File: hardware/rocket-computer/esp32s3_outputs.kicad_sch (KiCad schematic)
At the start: 43 parts, among them J5 Conn_01x04, SW3 R-667995, U11 GD5F2GQ5UEYIGR, U13 GD25Q128ESIG, U14 479480001, U15 ESP32-S3RH2, U29 TPS22810DRVR, Y1 ABS07-32.768KHZ-T, Y2 ECS-400-10-37B2-CKY-TR

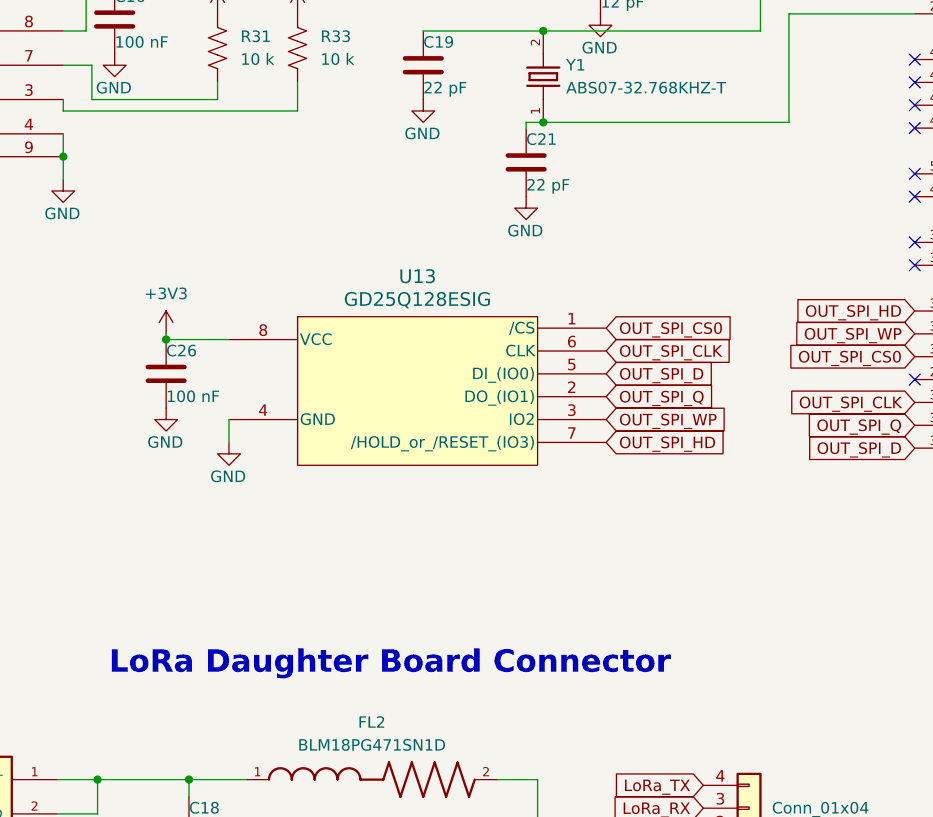
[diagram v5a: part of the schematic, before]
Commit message: hardware(V10): the part swaps the mini got and this board never did — both boot NORs, the pyro FETs, the magnetometer and the barometer (#1452)
v10-power-parity-2026-09-11.md closed the *circuit* differences between the
two boards, measuring forward from the TPS61094 rework (2026-08-29). It never
looked further back, and the *part* swaps in a4667604 (2026-08-16,
"hardware(minis): cost-reduction part swaps") only ever touched the two mini
boards. Two of that commit's six items had since arrived here by other routes
(DTC123JETL on 09-05, the PA0805 shunt); the rest had not.

Carried over:

- U13/U16 boot NOR: GD25Q128ESIG SOIC-8 208 mil -> W25Q128JVYIQ 24-ball WLCSP,
  the part the mini moved to on 2026-09-04. Both placements keep every net;
  only the pad names change (1-8 -> ball designators). Both blocks redrawn so
  the pins land on their labels, and U16's /CS pull-up R46 now runs over the
  top of the part into the VCC node.
- U6/U7/U8/U10 pyro high-side P-FETs: TPN4R712MD -> Winsok WSD20L50DN33. The
  incumbent is unbuyable at build quantity until the Q4-2026 Mouser restock;
  land compatibility was closed on the mini by numeric overlay of the vendor
  drawing. Same footprint, same 8-pin geometry, pins typed passive instead of
  unspecified.
- U9 pyro-ARM N-FET: CSD16323Q3 -> AOS AON7534. Same pinout, same land, and
  the mini keeps the CSD16323Q3 symbol for it, so this is fields only.
- U3 magnetometer: IIS2MDCTR LGA-12 2x2 -> QST QMC5883P LGA-16 3x3, with C6
  220 nF -> 10 uF for the C1 reservoir. Not pad-for-pad: IIS2MDCTR_SCL/SDA
  become MAG_SCL/MAG_SDA (the mini's names — they name the slot, not the part
  in it), the QMC land exposes no DRDY/INT pad so IIS2MDCTR_INT is gone and P4
  GPIO46 is free with a no-connect on it, and the ST part's separate VDD_IO and
  its CS strap to V_MCU_SWTCH go with it.
- U4 barometer: BMP585 LGA-9 -> BMP581 LGA-10 2x2. A drop-in on the drawing —
  the two symbols are built to the same pin grid, so U4 keeps its placement and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
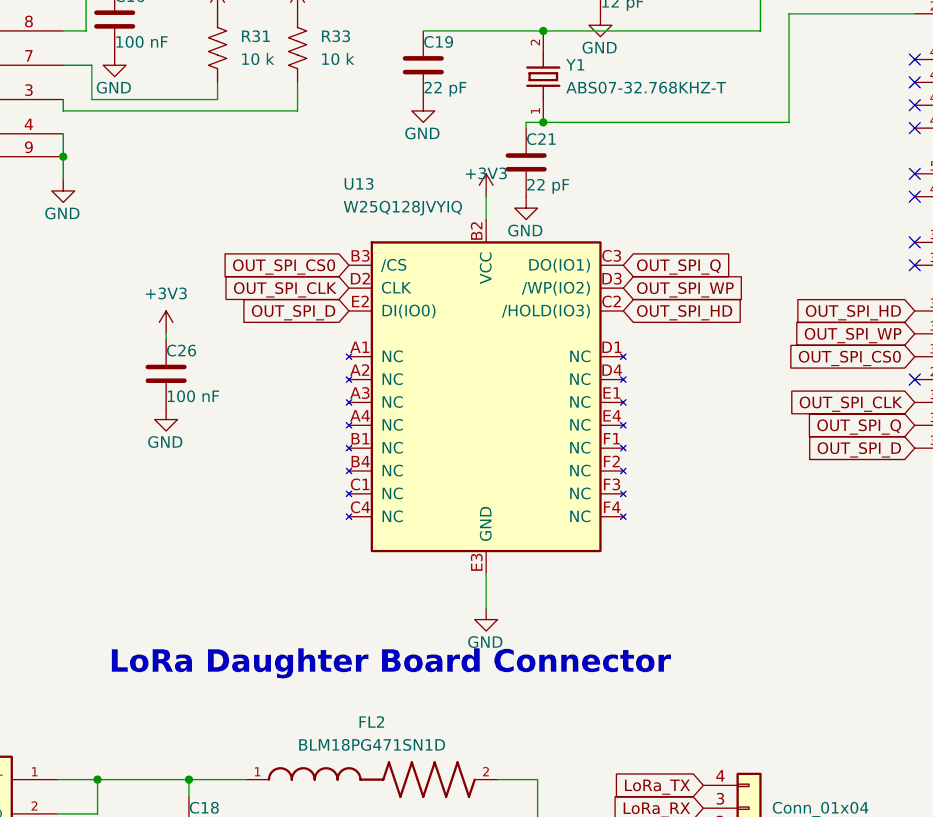
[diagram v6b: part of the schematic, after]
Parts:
- C18: MPN CL21A226MOQNNNE -> CL21A226KOQNNNE
- U13: value GD25Q128ESIG -> W25Q128JVYIQ; footprint Footprints:SOIC127P790X216-8N -> Footprints:24-WLCSP_Y_WIN; symbol Custom:W25Q128JVSIQ -> Custom:W25Q128JVYIQ; MPN GD25Q128ESIG -> W25Q128JVYIQ; Mfr GigaDevice -> Winbond
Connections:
- net +3V3: now also U13.B2 (VCC); no longer U13.8 (VCC)
- net GND: now also U13.E3 (GND); no longer U13.4 (GND)
- net OUT_SPI_CLK: now also U13.D2 (CLK); no longer U13.6 (CLK)
- net OUT_SPI_CS0: now also U13.B3 (/CS); no longer U13.1 (/CS)
- net OUT_SPI_D: now also U13.E2 (DI(IO0)); no longer U13.5 (DI_(IO0))
- net OUT_SPI_HD: now also U13.C2 (/HOLD(IO3)); no longer U13.7 (/HOLD_or_/RESET_(IO3))
- net OUT_SPI_Q: now also U13.C3 (DO(IO1)); no longer U13.2 (DO_(IO1))
- net OUT_SPI_WP: now also U13.D3 (/WP(IO2)); no longer U13.3 (IO2)
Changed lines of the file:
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@@
 		(color 0 0 0 0)
 	)
-	(junction
-		(at 78.74 104.775)
-		(diameter 0)
-		(color 0 0 0 0)
-	)
 	(wire
 		(pts
@@
 	(wire
 		(pts
-			(xy 85.725 113.665) (xy 85.725 116.205)
-		)
-		(stroke
-			(width 0)
-			(type default)
-		)
-	)
-	(wire
-		(pts
 			(xy 81.28 153.67) (xy 87.63 153.67)
 		)
@@
 	(wire
 		(pts
-			(xy 78.74 104.775) (xy 85.725 104.775)
-		)
-		(stroke
-			(width 0)
-			(type default)
-		)
-	)
-	(wire
-		(pts
 			(xy 161.925 66.04) (xy 144.78 66.04)
 		)
@@
 	(global_label "OUT_SPI_CS0"
 		(shape input)
-		(at 127.635 103.505 0)
+		(at 99.06 96.52 180)
 		(fields_autoplaced yes)
 		(effects
@@
 				(size 1.27 1.27)
 			)
-			(justify left)
+			(justify right)
 		)
 		(property "Intersheetrefs" "${INTERSHEET_REFS}"
-			(at 142.9573 103.505 0)
+			(at 83.7377 96.52 0)
 			(hide yes)
 			(show_name no)
@@
 					(size 1.27 1.27)
 				)
-				(justify left)
+				(justify right)
 			)
 		)
@@
 	(global_label "OUT_SPI_CLK"
 		(shape input)
-		(at 127.635 106.045 0)
+		(at 99.06 99.06 180)
 		(fields_autoplaced yes)
 		(effects
@@
 				(size 1.27 1.27)
 			)
-			(justify left)
+			(justify right)
 		)
 		(property "Intersheetrefs" "${INTERSHEET_REFS}"
-			(at 142.8364 106.045 0)
+			(at 83.8586 99.06 0)
 			(hide yes)
 			(show_name no)
@@
 					(size 1.27 1.27)
 				)
-				(justify left)
+				(justify right)
 			)
 		)
@@
 	(global_label "OUT_SPI_WP"
 		(shape input)
-		(at 127.635 113.665 0)
+		(at 129.54 99.06 0)
 		(fields_autoplaced yes)
 		(effects
@@
 		)
 		(property "Intersheetrefs" "${INTERSHEET_REFS}"
-			(at 141.9897 113.665 0)
+			(at 143.8947 99.06 0)
 			(hide yes)
 			(show_name no)
@@
 	(global_label "OUT_SPI_Q"
 		(shape input)
-		(at 127.635 111.125 0)
+		(at 129.54 96.52 0)
 		(fields_autoplaced yes)
 		(effects
@@
 		)
 		(property "Intersheetrefs" "${INTERSHEET_REFS}"
-			(at 140.5988 111.125 0)
+			(at 142.5038 96.52 0)
 			(hide yes)
 			(show_name no)
@@
 	(global_label "OUT_SPI_D"
 		(shape input)
-		(at 127.635 108.585 0)
+		(at 99.06 101.6 180)
 		(fields_autoplaced yes)
 		(effects
@@
 				(size 1.27 1.27)
 			)
-			(justify left)
+			(justify right)
 		)
 		(property "Intersheetrefs" "${INTERSHEET_REFS}"
-			(at 140.5383 108.585 0)
+			(at 86.1567 101.6 0)
 			(hide yes)
 			(show_name no)
@@
 					(size 1.27 1.27)
 				)
-				(justify left)
+				(justify right)
 			)
 		)
@@
 	(global_label "OUT_SPI_HD"
 		(shape input)
-		(at 127.635 116.205 0)
+		(at 129.54 101.6 0)
 		(fields_autoplaced yes)
 		(effects
@@
 		)
 		(property "Intersheetrefs" "${INTERSHEET_REFS}"
-			(at 141.8688 116.205 0)
+			(at 143.7738 101.6 0)
 			(hide yes)
 			(show_name no)
@@
 		)
 	)
-	(symbol
-		(lib_id "Custom:W25Q128JVSIQ")
-		(at 62.865 109.855 0)
+		(symbol
+		(lib_id "Custom:W25Q128JVYIQ")
+		(at 114.3 104.14 0)
 		(unit 1)
 		(body_style 1)
@@
 		(in_pos_files yes)
 		(dnp no)
-		(fields_autoplaced yes)
 		(property "Reference" "U13"
-			(at 106.68 97.79 0)
+			(at 98.425 88.265 0)
 			(show_name no)
 			(do_not_autoplace no)
 			(effects
 				(font
-					(size 1.524 1.524)
+					(size 1.27 1.27)
 				)
+				(justify left bottom)
 			)
 		)
-		(property "Value" "GD25Q128ESIG"
-			(at 106.68 100.33 0)
+		(property "Value" "W25Q128JVYIQ"
+			(at 98.425 90.805 0)
 			(show_name no)
 			(do_not_autoplace no)
 			(effects
 				(font
-					(size 1.524 1.524)
+					(size 1.27 1.27)
 				)
+				(justify left bottom)
 			)
 		)
-		(property "Footprint" "Footprints:SOIC127P790X216-8N"
-			(at 62.865 109.855 0)
+		(property "Footprint" "Footprints:24-WLCSP_Y_WIN"
+			(at 127 102.87 0)
 			(hide yes)
 			(show_name no)
@@
 				(font
 					(size 1.27 1.27)
-					(italic yes)
 				)
+				(justify left bottom)
 			)
 		)
 		(property "Datasheet" ""
-			(at 62.865 109.855 0)
+			(at 114.3 104.14 0)
 			(hide yes)
 			(show_name no)
@@
 				(font
 					(size 1.27 1.27)
-					(italic yes)
 				)
+				(justify left bottom)
 			)
 		)
-		(property "Description" ""
-			(at 62.865 109.855 0)
+		(property "Description" "128 Mbit serial NOR flash, quad SPI, 2.7-3.6 V, 24-ball WLCSP"
+			(at 114.3 104.14 0)
 			(hide yes)
 			(show_name no)
@@
 					(size 1.27 1.27)
 				)
+				(justify left bottom)
 			)
 		)
-		(property "MPN" "GD25Q128ESIG"
-			(at 62.865 109.855 0)
+		(property "MPN" "W25Q128JVYIQ"
+			(at 114.3 104.14 0)
 			(hide yes)
 			(show_name no)
@@
 					(size 1.27 1.27)
 				)
+				(justify left bottom)
 			)
 		)
-		(property "Mfr" "GigaDevice"
-			(at 62.865 109.855 0)
+		(property "Mfr" "Winbond"
+			(at 114.3 104.14 0)
 			(hide yes)
 			(show_name no)
@@
 					(size 1.27 1.27)
 				)
+				(justify left bottom)
 			)
 		)
-		(pin "8"
+		(pin "A1"
 		)
-		(pin "4"
+		(pin "A2"
 		)
-		(pin "2"
+		(pin "A3"
 		)
-		(pin "3"
+		(pin "A4"
 		)
-		(pin "5"
+		(pin "B1"
 		)
-		(pin "6"
+		(pin "B2"
 		)
-		(pin "7"
+		(pin "B3"
 		)
-		(pin "1"
+		(pin "B4"
+		)
+		(pin "C1"
+		)
+		(pin "C2"
+		)
+		(pin "C3"
+		)
+		(pin "C4"
+		)
+		(pin "D1"
+		)
+		(pin "D2"
+		)
+		(pin "D3"
+		)
+		(pin "D4"
+		)
+		(pin "E1"
+		)
+		(pin "E2"
+		)
+		(pin "E3"
+		)
+		(pin "E4"
+		)
+		(pin "F1"
+		)
+		(pin "F2"
+		)
+		(pin "F3"
+		)
+		(pin "F4"
 		)
 		(instances
@@
 	(symbol
 		(lib_id "power:GND")
-		(at 85.725 116.205 0)
+		(at 114.3 134.62 0)
 		(unit 1)
 		(body_style 1)
@@
 		(dnp no)
 		(property "Reference" "#PWR054"
-			(at 85.725 122.555 0)
+			(at 114.3 140.97 0)
 			(hide yes)
 			(show_name no)
@@
 		)
 		(property "Value" "GND"
-			(at 87.63 120.015 0)
+			(at 116.205 138.43 0)
 			(show_name no)
 			(do_not_autoplace no)
@@
 		)
 		(property "Footprint" ""
-			(at 85.725 116.205 0)
+			(at 114.3 134.62 0)
 			(hide yes)
 			(show_name no)
@@
 		)
 		(property "Datasheet" ""
-			(at 85.725 116.205 0)
+			(at 114.3 134.62 0)
 			(hide yes)
 			(show_name no)
@@
 		)
 		(property "Description" "Power symbol creates a global label with name \"GND\" , ground"
-			(at 85.725 116.205 0)
+			(at 114.3 134.62 0)
 			(hide yes)
 			(show_name no)
@@
 			)
 		)
-		(property "MPN" "CL21A226MOQNNNE"
+		(property "MPN" "CL21A226KOQNNNE"
 			(at 81.28 159.385 0)
 			(hide yes)
@@
 		(at 161.925 86.36)
 	)
+	(wire
+		(pts
+			(xy 114.3 130.81) (xy 114.3 134.62)
+		)
+		(stroke
+			(width 0)
+			(type default)
+		)
+	)
+	(wire
+		(pts
+			(xy 114.3 91.44) (xy 114.3 88.9)
+		)
+		(stroke
+			(width 0)
+			(type default)
+		)
+	)
+	(symbol
+		(lib_id "power:+3V3")
+		(at 114.3 88.9 0)
+		(unit 1)
+		(body_style 1)
+		(exclude_from_sim no)
+		(in_bom yes)
+		(on_board yes)
+		(in_pos_files yes)
+		(dnp no)
+		(fields_autoplaced yes)
+		(property "Reference" "#PWR0712"
+			(at 114.3 85.344 0)
+			(hide yes)
+			(show_name no)
+			(do_not_autoplace no)
+			(effects
+				(font
+					(size 1.27 1.27)
+				)
+			)
+		)
+		(property "Value" "+3V3"
+			(at 114.3 86.36 0)
+			(show_name no)
+			(do_not_autoplace no)
+			(effects
+				(font
+					(size 1.27 1.27)
+				)
+			)
+		)
+		(property "Footprint" ""
+			(at 114.3 88.9 0)
+			(hide yes)
+			(show_name no)
+			(do_not_autoplace no)
+			(effects
+				(font
+					(size 1.27 1.27)
+				)
+			)
+		)
+		(property "Datasheet" ""
+			(at 114.3 88.9 0)
+			(hide yes)
+			(show_name no)
+			(do_not_autoplace no)
+			(effects
+				(font
+					(size 1.27 1.27)
+				)
+			)
+		)
+		(property "Description" ""
+			(at 114.3 88.9 0)
+			(hide yes)
+			(show_name no)
+			(do_not_autoplace no)
+			(effects
+				(font
+					(size 1.27 1.27)
+				)
+			)
+		)
+		(pin "1"
+		)
+		(instances
+			(project "rocket-computer"
+				(path "/ae61c2c4-72e9-4776-93ae-2e716b9dc70f/eab70588-b031-4461-adac-e038e88381cb"
+					(reference "#PWR0712")
+					(unit 1)
+				)
+			)
+		)
+	)
 )

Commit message: hardware(V10): the 22 uF 0805 goes back to the M-code, which is the grade the fleet actually buys
3ce1d38d moved the V10's twelve 22 uF 0805 from CL21A226MOQNNNE to
CL21A226KOQNNNE on the grounds that the mini uses the K grade. The mini does,
in its schematic — but the priced CrossBoard BOM retired that line on
2026-08-28 and merged both minis back onto the M-code, because the K repriced
UP to $0.1257@2000 while the M-code sibling sells at $0.0725. So the parity
argument was reading a stale source: the sourcing decision had already gone the
other way, and nothing anywhere claims the K's tighter +/-10% tolerance is
needed at any of these sites.

All twelve placements (C7, C8, C9, C10, C11, C13, C14, C17, C18, C43, C141,
C144) revert to CL21A226MOQNNNE — same Samsung series, same 0805, same 16 V,
which is what the >=16 V requirement on the 2S rails asks for. Ten of the
twelve are placed on the board and take the field change there too; C141 and
C144 are among the parts still waiting to be placed.

Note for whoever next touches the mini: its schematic is now the odd one out
and should follow the same way.

Measured: field-only change. Netlist component count unchanged at 277, every
net identical. kicad-cli pcb drc --severity-all --schematic-parity unchanged at
162 violations and 97 parity items. bom.csv regenerated and reconciled to the
schematic across all 265 designators. check_docs.py clean.

Co-Authored-By: Claude Opus 5 <noreply@anthropic.com>
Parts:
- C18: MPN CL21A226KOQNNNE -> CL21A226MOQNNNE
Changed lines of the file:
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@@
 			)
 		)
-		(property "MPN" "CL21A226KOQNNNE"
+		(property "MPN" "CL21A226MOQNNNE"
 			(at 81.28 159.385 0)
 			(hide yes)
